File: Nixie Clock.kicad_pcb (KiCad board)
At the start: 2 copper layers, 122.2 x 42.4 mm, 42 parts, among them J1 USB_C_Receptacle_USB2.0, Q1 FDS2672CT, Q26 MMBTA42, U1 ESP32-S2-WROVER, U1 UCC3803

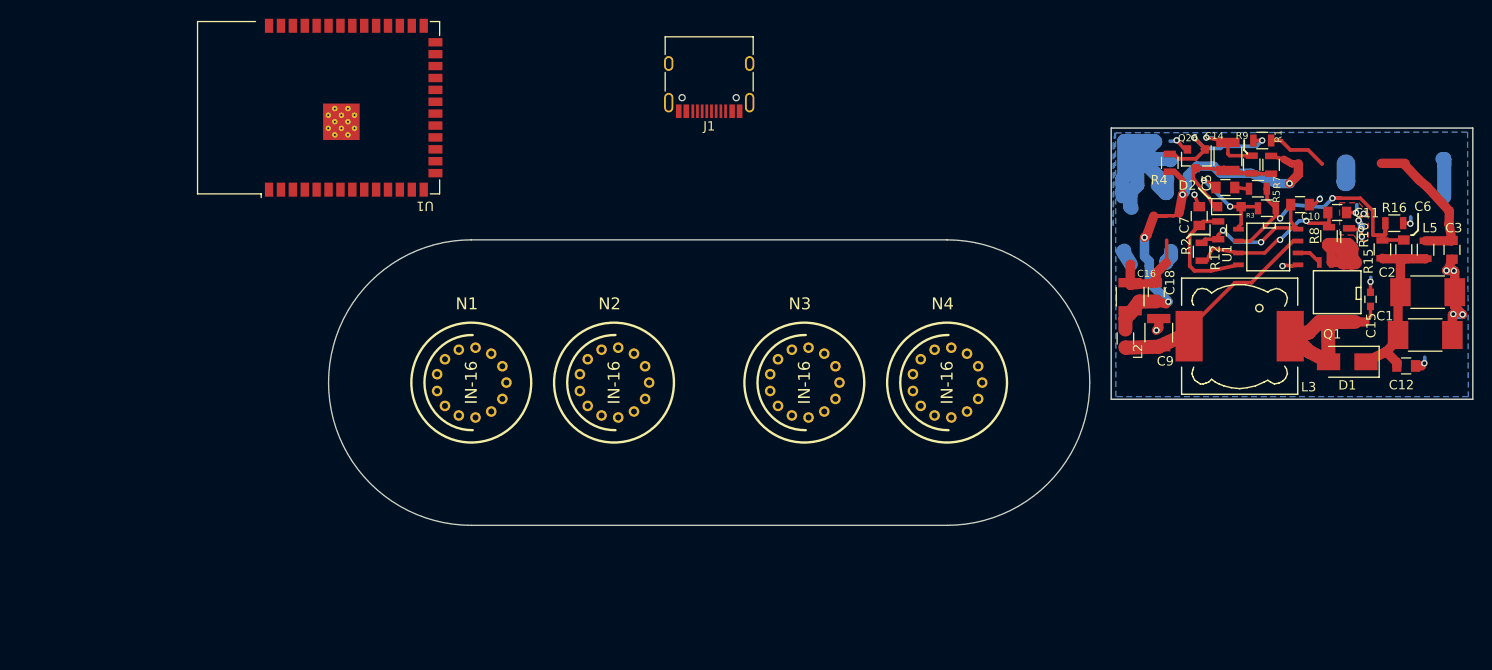
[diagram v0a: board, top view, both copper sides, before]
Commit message: Created top plate ideas
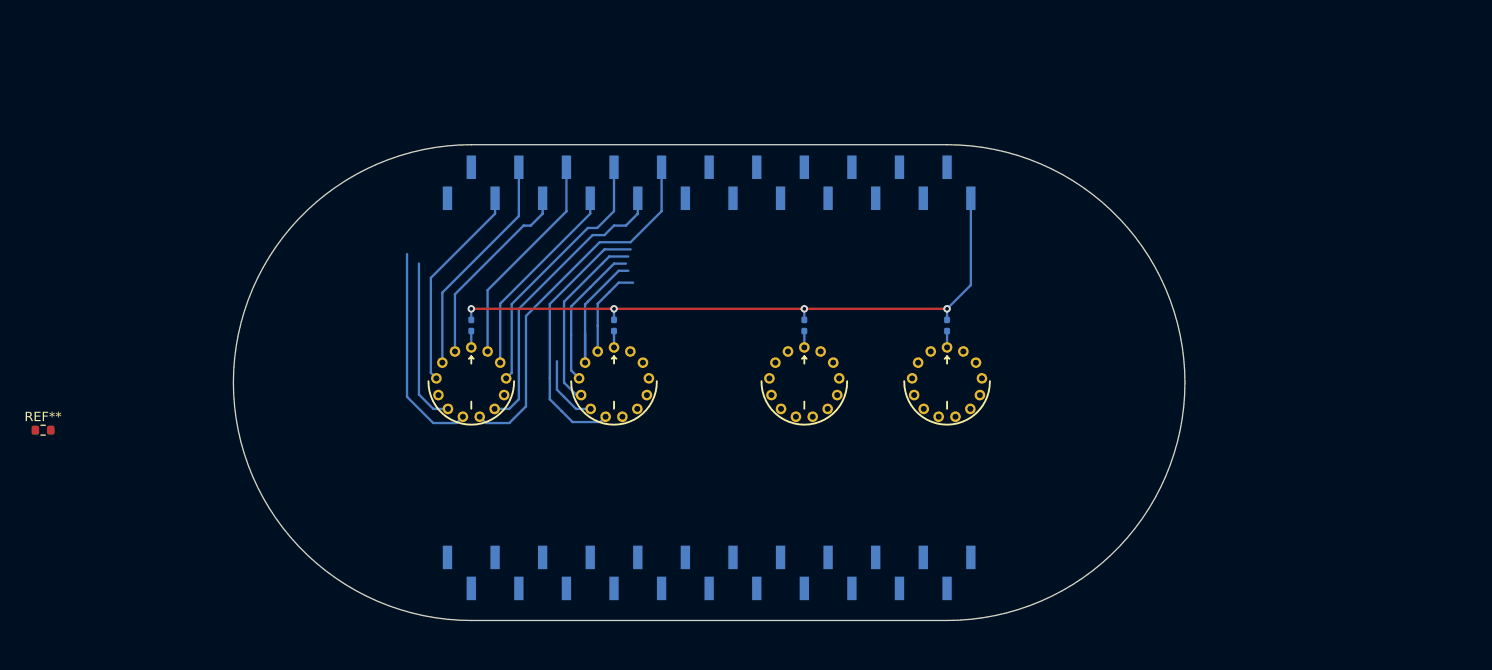
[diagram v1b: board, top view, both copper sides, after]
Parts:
- removed C1, C2: 1uF 250v, Capacitors_SMD:C_1812_HandSoldering
- removed C10: 0.1uF 16v, Capacitors_SMD:C_0805
- removed C11: 1nF, Capacitors_SMD:C_0805
- removed C12, C3: 0.1uF 250v, Capacitors_SMD:C_0805
- removed C14: 47uF 16v, Capacitors_SMD:C_1210
- removed C15: 560pF 250v, Capacitors_SMD:C_0603
- removed C16, C9: 100uF 16v, Capacitors_SMD:C_1210
- removed C18: 0.1uF, Capacitors_SMD:C_0805
- removed C5: 220pF, Capacitors_SMD:C_0805
- removed C6: 100pF 250v, Capacitors_SMD:C_0805
- removed C7: 430pF, Capacitors_SMD:C_0805
- removed D1: ES1D, Diodes_SMD:D_SMA
- removed D2: BAT54, Diodes_SMD:D_SOD-323_HandSoldering
- removed G***: LOGO, Symbol:copyright
- removed G***: OSHW_logo_silkscreen-front_5mm, NixieSupply5vto170vDCMBoostMini_socket:OSHW_logo_silkscreen-front_5mm
- removed L2, L5: 60ohm 100Mhz, Resistors_SMD:R_0805
- removed L3: 33uH, NixieSupply5vto160vDCMBoost_socket:Choke_SMD_12x12mm_Wurth_WE-PD
- removed N1, N2, N3, N4: IN-16, nixies-us:nixies-us-IN-16
- removed Q1: FDS2672CT, etaclock:SOIC-8-N
- removed Q26: MMBTA42, TO_SOT_Packages_SMD:SOT-23
- removed R10: 0.1 1/2W, Resistors_SMD:R_0805
- removed R12: 4.12k, Resistors_SMD:R_0805
- removed R15: 634k, Resistors_SMD:R_0805
- removed R16: 7.68k, Resistors_SMD:R_0805
- removed R5: 0 Ohm, Resistors_SMD:R_0805
- removed R7: 2k, Resistors_SMD:R_0805
- removed R8: 1k, Resistors_SMD:R_0805
- removed R9: 100k, Resistors_SMD:R_0805
- removed U1: ESP32-S2-WROVER, RF_Module:ESP32-S3-WROOM-1
- removed U1: UCC3803, NixieSupply5vto160vDCMBoost_socket:SOIC-8-N
- added IN1: ~, Indicator-Tube:IN-16, F.Cu at (152.4, 83.8)
- added IN2: ~, Indicator-Tube:IN-16, F.Cu at (167.6, 83.8)
- added IN3: ~, Indicator-Tube:IN-16, F.Cu at (188.0, 83.8)
- added IN4: ~, Indicator-Tube:IN-16, F.Cu at (203.2, 83.8)
- added J2: Conn_01x23_Pin, Connector_PinHeader_2.54mm:PinHeader_1x23_P2.54mm_Vertical_SMD_Pin1Left, B.Cu at (177.8, 104.1)
- added REF**: R_0603_1608Metric, Resistor_SMD:R_0603_1608Metric, F.Cu at (106.7, 88.9)
- J1: value USB_C_Receptacle_USB2.0 -> Conn_01x23_Pin; footprint Connector_USB:USB_C_Receptacle_HRO_TYPE-C-31-M-12 -> Connector_PinHeader_2.54mm:PinHeader_1x23_P2.54mm_Vertical_SMD_Pin1Left; moved to B.Cu
- R1: value 1k -> 33k; footprint Resistors_SMD:R_0805 -> Resistor_SMD:R_0402_1005Metric_Pad0.72x0.64mm_HandSolder; moved to B.Cu
- R2: value 60.4k -> 33k; footprint Resistors_SMD:R_0805 -> Resistor_SMD:R_0402_1005Metric_Pad0.72x0.64mm_HandSolder; moved to B.Cu
- R3: value N.U. -> 33k; footprint Resistors_SMD:R_0805 -> Resistor_SMD:R_0402_1005Metric_Pad0.72x0.64mm_HandSolder; moved to B.Cu
- R4: value 100k -> 33k; footprint Resistors_SMD:R_0805 -> Resistor_SMD:R_0402_1005Metric_Pad0.72x0.64mm_HandSolder; moved to B.Cu
- moved R1 86.7 mm to (152.4, 77.7), turned to 90 degrees
- moved R2 65.3 mm to (167.6, 77.7), turned to 90 degrees
- moved R3 51.0 mm to (188.0, 77.7), turned to 90 degrees
- moved R4 29.4 mm to (203.2, 77.7), turned to 90 degrees
- moved J1 11.7 mm to (177.8, 62.5), turned to 90 degrees
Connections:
- R1 pad 1: (no net) -> Net-(IN1-PadA)
- R1 pad 2: (no net) -> +170v
- R2 pad 1: (no net) -> Net-(IN2-PadA)
- R2 pad 2: (no net) -> +170v
- R3 pad 1: (no net) -> Net-(IN3-PadA)
- R3 pad 2: (no net) -> +170v
- R4 pad 1: (no net) -> Net-(IN4-PadA)
- R4 pad 2: (no net) -> +170v
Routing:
- net (no net): track 361.3 -> 0.00 mm, vias 32 -> 0
- net +170v: track 0.00 -> 68.4 mm, vias 0 -> 4
- net 1_6: track 0.00 -> 39.4 mm
- net 1_2: track 0.00 -> 31.2 mm
- net 2_5: track 0.00 -> 28.4 mm
- net 1_8: track 0.00 -> 27.9 mm
- net 1_7: track 0.00 -> 24.2 mm
- net 1_0: track 0.00 -> 23.2 mm
- net 1_5: track 0.00 -> 22.6 mm
- net 1_3: track 0.00 -> 22.3 mm
- net 1_9: track 0.00 -> 21.5 mm
- net 1_1: track 0.00 -> 20.7 mm
- net RDP: track 0.00 -> 19.9 mm
- net 1_4: track 0.00 -> 17.7 mm
- net 2_3: track 0.00 -> 15.8 mm
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- removed copper zone on B.Cu, net (none)
- removed copper zone on F.Cu, net (none)
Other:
- board size 122.2 x 42.4 mm -> 101.6 x 50.8 mm
- board text removed: "Mark Smith 2018"
- board text removed: "NixieSupplyMini Rev3_1812"
- board text removed: "www.surfncircuits.com"

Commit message: Finished top plate
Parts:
- removed REF**: R_0603_1608Metric, Resistor_SMD:R_0603_1608Metric
- R1, R2, R3, R4: footprint Resistor_SMD:R_0402_1005Metric_Pad0.72x0.64mm_HandSolder -> Resistor_SMD:R_0805_2012Metric
- moved J2 1.02 mm to (177.8, 105.2)
- moved R1 0.89 mm to (152.4, 76.8)
- moved R3 0.89 mm to (188.0, 76.8)
- moved R4 0.89 mm to (203.2, 76.8)
- moved R2 0.76 mm to (167.6, 77.0)
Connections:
- J1 pad 10: unconnected-(J1-Pin_10-Pad10) -> 2_7
- J1 pad 11: unconnected-(J1-Pin_11-Pad11) -> 2_3
- J1 pad 12: unconnected-(J1-Pin_12-Pad12) -> 2_4
- J1 pad 13: unconnected-(J1-Pin_13-Pad13) -> 2_5
- J1 pad 4: unconnected-(J1-Pin_4-Pad4) -> 2_6
- J1 pad 5: unconnected-(J1-Pin_5-Pad5) -> 2_2
- J1 pad 6: unconnected-(J1-Pin_6-Pad6) -> 2_8
- J1 pad 7: unconnected-(J1-Pin_7-Pad7) -> 2_9
- J1 pad 8: unconnected-(J1-Pin_8-Pad8) -> 2_0
- J1 pad 9: unconnected-(J1-Pin_9-Pad9) -> 2_1
- J2 pad 1: unconnected-(J2-Pin_1-Pad1) -> GND
- J2 pad 10: unconnected-(J2-Pin_10-Pad10) -> 3_8
- J2 pad 11: unconnected-(J2-Pin_11-Pad11) -> 3_9
- J2 pad 12: unconnected-(J2-Pin_12-Pad12) -> 3_0
- J2 pad 13: unconnected-(J2-Pin_13-Pad13) -> 4_1
- J2 pad 14: unconnected-(J2-Pin_14-Pad14) -> 4_7
- J2 pad 15: unconnected-(J2-Pin_15-Pad15) -> 4_3
- J2 pad 16: unconnected-(J2-Pin_16-Pad16) -> 4_4
- J2 pad 17: unconnected-(J2-Pin_17-Pad17) -> 4_5
- J2 pad 18: unconnected-(J2-Pin_18-Pad18) -> 4_6
- J2 pad 19: unconnected-(J2-Pin_19-Pad19) -> 4_2
- J2 pad 2: unconnected-(J2-Pin_2-Pad2) -> 3_1
- J2 pad 20: unconnected-(J2-Pin_20-Pad20) -> 4_8
- J2 pad 21: LDP -> 4_9
- J2 pad 22: GND -> 4_0
- J2 pad 23: +5V -> GND
- J2 pad 3: unconnected-(J2-Pin_3-Pad3) -> 3_7
- J2 pad 4: unconnected-(J2-Pin_4-Pad4) -> 3_3
- J2 pad 5: unconnected-(J2-Pin_5-Pad5) -> 3_4
- J2 pad 6: unconnected-(J2-Pin_6-Pad6) -> 3_5
- J2 pad 7: unconnected-(J2-Pin_7-Pad7) -> 3_6
- J2 pad 8: unconnected-(J2-Pin_8-Pad8) -> 3_2
- J2 pad 9: unconnected-(J2-Pin_9-Pad9) -> LDP
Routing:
- net 3_1: track 0.00 -> 47.5 mm
- net 2_6: track 0.00 -> 45.9 mm
- net 3_0: track 0.00 -> 40.2 mm
- net 3_7: track 0.00 -> 39.3 mm
- net 3_3: track 0.00 -> 38.7 mm
- net 3_8: track 0.00 -> 36.2 mm
- net 4_1: track 0.00 -> 36.1 mm
- net RDP: track 19.9 -> 55.4 mm, vias 0 -> 2
- net 3_2: track 0.00 -> 34.9 mm
- net 3_5: track 0.00 -> 34.8 mm
- net 2_2: track 0.00 -> 34.8 mm
- net 3_9: track 0.00 -> 34.2 mm
- net 4_7: track 0.00 -> 34.0 mm
- net 4_0: track 0.00 -> 33.6 mm
- net 2_8: track 0.00 -> 33.2 mm
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- added copper zone on B.Cu, net GND
- added copper zone on F.Cu, net GND
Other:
- outline, holes or cut-outs redrawn
